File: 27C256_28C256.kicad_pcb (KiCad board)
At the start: 2 copper layers, 16.4 x 34.2 mm, 3 parts, among them J1 27C256 DIP LEGS, U1 28C256

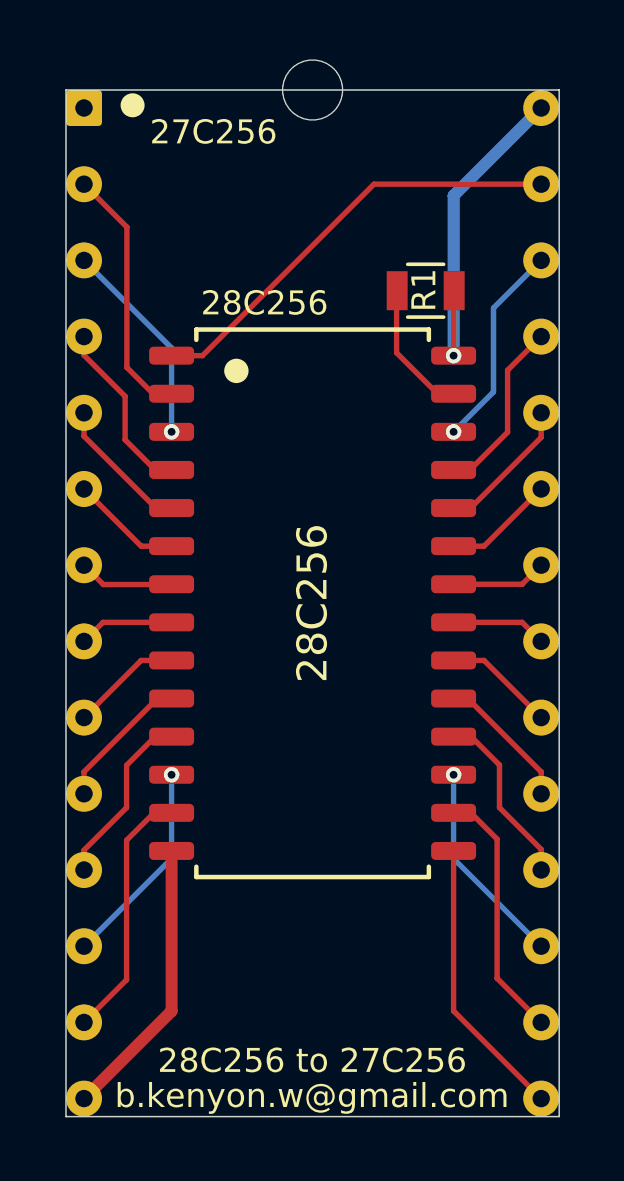
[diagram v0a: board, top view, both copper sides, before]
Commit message: 27C256_28C256: add jumpers to allow programming without needing a test clip
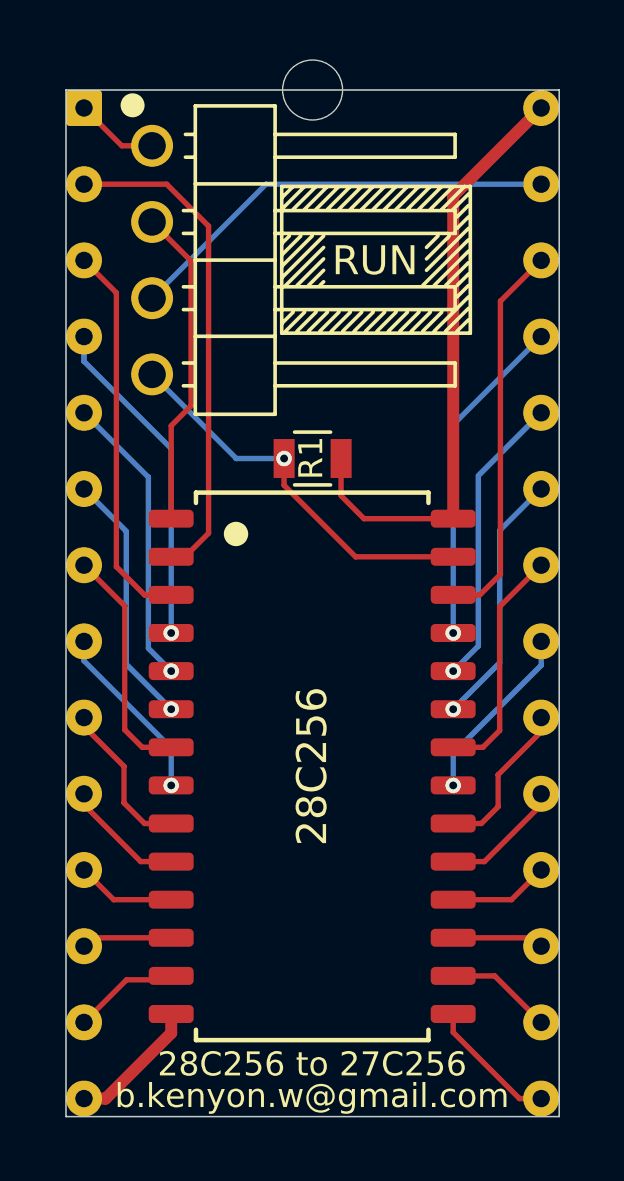
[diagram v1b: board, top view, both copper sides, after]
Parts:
- added JP1: Jumper_3_Bridged12, 000_LOCAL:Pin_Header_Angled_1x04_Pitch2.54mm, F.Cu at (144.7, 84.8)
- moved R1 6.75 mm to (150.0, 95.2)
- moved U1 5.44 mm to (150.0, 105.4)
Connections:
- J1 pad 1: (no net) -> /NC_A14
- J1 pad 27: /A14 -> /A14_WE
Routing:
- net /A14_WE: track 0.00 -> 14.5 mm
- net /VCC: track 11.6 -> 20.2 mm, vias 1 -> 0
- net /~WE: track 4.54 -> 13.1 mm, vias 0 -> 1
- net /A12: track 8.55 -> 16.5 mm
- net /A13: track 6.92 -> 12.9 mm, vias 1 -> 0
- net /A7: track 6.92 -> 12.9 mm, vias 1 -> 0
- net /A5: track 4.69 -> 9.81 mm, vias 0 -> 1
- net /A8: track 5.97 -> 11.1 mm, vias 0 -> 1
- net /A6: track 5.97 -> 11.1 mm, vias 0 -> 1
- net /A9: track 4.72 -> 9.83 mm, vias 0 -> 1
- net /GND: track 9.46 -> 4.45 mm
- net /D3: track 9.46 -> 4.46 mm
- net /D2: track 8.54 -> 3.55 mm
- net /D4: track 8.53 -> 3.57 mm
- net /A11: track 3.71 -> 8.56 mm, vias 0 -> 1
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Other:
- board text added: "27C256 pinout (RUN)"
- board text added: "28C256 pinout (PROGRAM)"
- board text added: "RUN"
- board text removed: "27C256"
- board text removed: "28C256"

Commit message: pours and text
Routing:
- net /A6: track 11.1 -> 19.0 mm
- net /A8: track 11.1 -> 13.4 mm
- net /A12: track 16.5 -> 17.8 mm
- net /A13: track 12.9 -> 13.5 mm
- net /GND: vias 0 -> 3
- added copper zone on B.Cu, net /GND
- added copper zone on F.Cu, net /GND
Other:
- board text added: "27C256 to 28C256"
- board text added: "github.com/bkw777/aDIPters"
- board text removed: "28C256 to 27C256"
- board text removed: "b.kenyon.w@gmail.com"

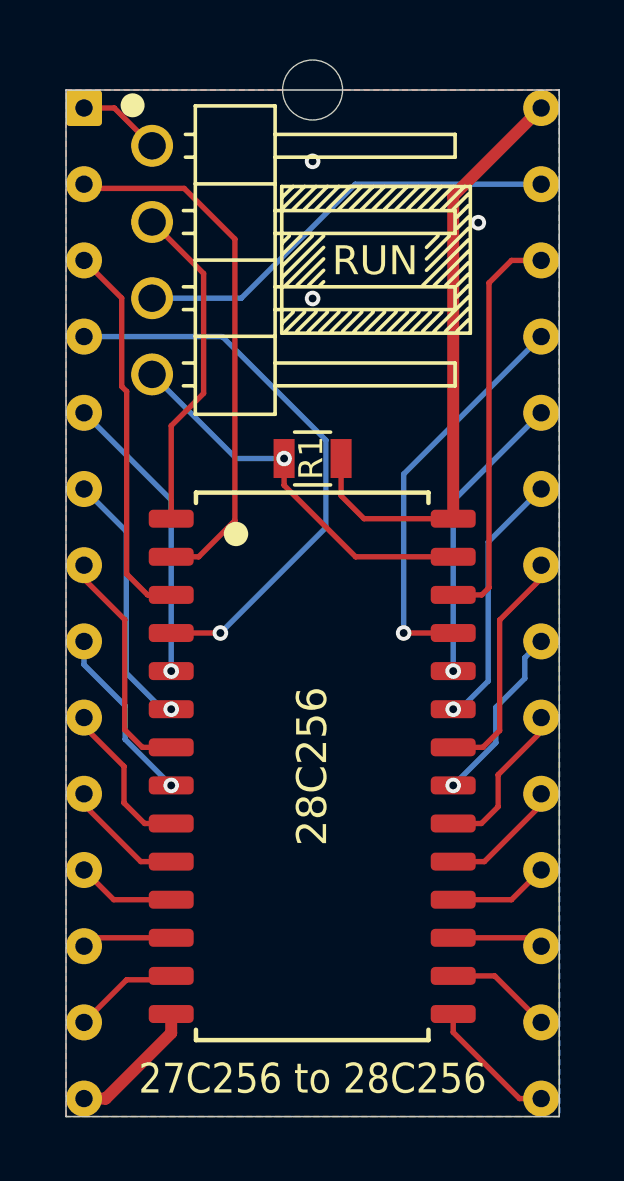
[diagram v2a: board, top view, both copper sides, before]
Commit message: improve copper pour
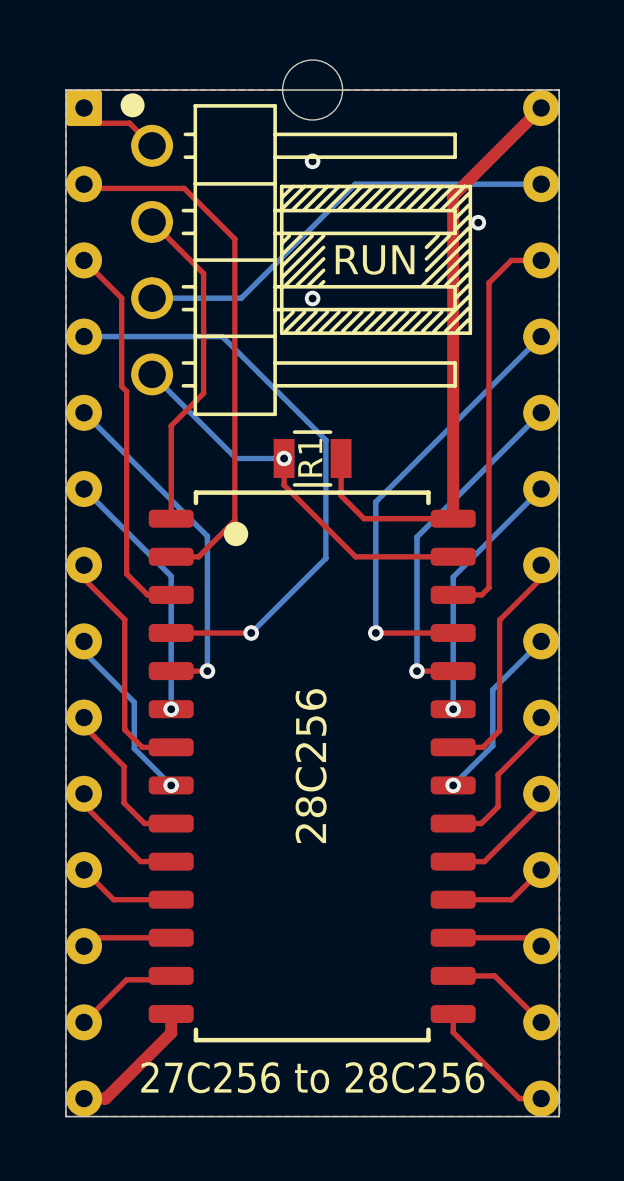
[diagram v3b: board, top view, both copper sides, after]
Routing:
- net /A9: track 9.83 -> 11.5 mm
- net /A5: track 9.81 -> 11.5 mm
- net /A8: track 13.4 -> 14.7 mm
- net /A6: track 19.0 -> 19.6 mm
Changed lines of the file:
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@@
     (thickness 1.6)
     (drawings 84)
-    (tracks 122)
+    (tracks 119)
     (zones 0)
     (modules 4)
@@
   )
   (setup
-    (last_trace_width 0.25)
+    (last_trace_width 0.18)
     (user_trace_width 0.16)
     (user_trace_width 0.18)
@@
   (segment (start 142.6596 111.1504) (end 142.38 111.43) (width 0.18) (layer F.Cu) (net 6))
   (segment (start 145.287 111.1504) (end 142.6596 111.1504) (width 0.18) (layer F.Cu) (net 6))
-  (via (at 153.035 100.9904) (size 0.52) (drill 0.26) (layers F.Cu B.Cu) (net 7))
-  (segment (start 153.035 95.695) (end 157.62 91.11) (width 0.18) (layer B.Cu) (net 7))
-  (segment (start 153.035 100.9904) (end 153.035 95.695) (width 0.18) (layer B.Cu) (net 7))
-  (segment (start 153.035 100.9904) (end 154.687 100.9904) (width 0.18) (layer F.Cu) (net 7))
+  (via (at 152.1079 100.9904) (size 0.52) (drill 0.26) (layers F.Cu B.Cu) (net 7))
+  (segment (start 152.1079 100.9904) (end 154.687 100.9904) (width 0.18) (layer F.Cu) (net 7))
+  (segment (start 152.1079 96.6221) (end 157.62 91.11) (width 0.18) (layer B.Cu) (net 7))
+  (segment (start 152.1079 100.9904) (end 152.1079 96.6221) (width 0.18) (layer B.Cu) (net 7))
   (segment (start 143.3704 109.8804) (end 145.287 109.8804) (width 0.18) (layer F.Cu) (net 8))
   (segment (start 142.38 108.89) (end 143.3704 109.8804) (width 0.18) (layer F.Cu) (net 8))
-  (via (at 154.687 102.2604) (size 0.52) (drill 0.26) (layers F.Cu B.Cu) (net 9))
-  (segment (start 154.687 96.583) (end 157.62 93.65) (width 0.18) (layer B.Cu) (net 9))
-  (segment (start 154.687 102.2604) (end 154.687 96.583) (width 0.18) (layer B.Cu) (net 9))
+  (via (at 153.4795 102.2604) (size 0.52) (drill 0.26) (layers F.Cu B.Cu) (net 9))
+  (segment (start 153.4795 102.2604) (end 154.687 102.2604) (width 0.18) (layer F.Cu) (net 9))
+  (segment (start 153.4795 97.7905) (end 157.62 93.65) (width 0.18) (layer B.Cu) (net 9))
+  (segment (start 153.4795 102.2604) (end 153.4795 97.7905) (width 0.18) (layer B.Cu) (net 9))
   (segment (start 142.38 106.7184) (end 142.38 106.35) (width 0.18) (layer F.Cu) (net 10))
   (segment (start 145.287 108.6104) (end 144.272 108.6104) (width 0.18) (layer F.Cu) (net 10))
   (segment (start 144.272 108.6104) (end 142.38 106.7184) (width 0.18) (layer F.Cu) (net 10))
   (via (at 154.687 103.5304) (size 0.52) (drill 0.26) (layers F.Cu B.Cu) (net 11))
-  (segment (start 155.8544 102.5906) (end 155.8544 97.9556) (width 0.18) (layer B.Cu) (net 11))
-  (segment (start 154.687 103.5304) (end 154.9146 103.5304) (width 0.18) (layer B.Cu) (net 11))
-  (segment (start 155.8544 97.9556) (end 157.62 96.19) (width 0.18) (layer B.Cu) (net 11))
-  (segment (start 154.9146 103.5304) (end 155.8544 102.5906) (width 0.18) (layer B.Cu) (net 11))
+  (segment (start 154.687 99.123) (end 157.62 96.19) (width 0.18) (layer B.Cu) (net 11))
+  (segment (start 154.687 103.5304) (end 154.687 99.123) (width 0.18) (layer B.Cu) (net 11))
   (segment (start 143.7132 105.4354) (end 142.38 104.1022) (width 0.18) (layer F.Cu) (net 12))
   (segment (start 142.38 104.1022) (end 142.38 103.81) (width 0.18) (layer F.Cu) (net 12))
@@
   (segment (start 155.6766 104.8004) (end 156.2354 104.2416) (width 0.18) (layer F.Cu) (net 13))
   (via (at 145.287 106.0704) (size 0.52) (drill 0.26) (layers F.Cu B.Cu) (net 14))
-  (segment (start 142.38 102.0448) (end 142.38 101.27) (width 0.18) (layer B.Cu) (net 14))
-  (segment (start 143.7513 103.4161) (end 142.38 102.0448) (width 0.18) (layer B.Cu) (net 14))
-  (segment (start 145.287 106.0704) (end 143.7513 104.5347) (width 0.18) (layer B.Cu) (net 14))
-  (segment (start 143.7513 104.5347) (end 143.7513 103.4161) (width 0.18) (layer B.Cu) (net 14))
+  (segment (start 142.38 101.6257) (end 142.38 101.27) (width 0.18) (layer B.Cu) (net 14))
+  (segment (start 144.0561 103.3018) (end 142.38 101.6257) (width 0.18) (layer B.Cu) (net 14))
+  (segment (start 145.287 106.0704) (end 144.0561 104.8395) (width 0.18) (layer B.Cu) (net 14))
+  (segment (start 144.0561 104.8395) (end 144.0561 103.3018) (width 0.18) (layer B.Cu) (net 14))
   (via (at 154.687 106.0704) (size 0.52) (drill 0.26) (layers F.Cu B.Cu) (net 15))
-  (segment (start 157.0736 102.5017) (end 157.0736 101.8164) (width 0.18) (layer B.Cu) (net 15))
-  (segment (start 156.1084 103.4669) (end 157.0736 102.5017) (width 0.18) (layer B.Cu) (net 15))
-  (segment (start 154.687 106.0704) (end 156.1084 104.649) (width 0.18) (layer B.Cu) (net 15))
-  (segment (start 157.0736 101.8164) (end 157.62 101.27) (width 0.18) (layer B.Cu) (net 15))
-  (segment (start 156.1084 104.649) (end 156.1084 103.4669) (width 0.18) (layer B.Cu) (net 15))
+  (segment (start 156.0068 102.8832) (end 157.62 101.27) (width 0.18) (layer B.Cu) (net 15))
+  (segment (start 154.687 106.0704) (end 156.0068 104.7506) (width 0.18) (layer B.Cu) (net 15))
+  (segment (start 156.0068 104.7506) (end 156.0068 102.8832) (width 0.18) (layer B.Cu) (net 15))
   (segment (start 142.38 99.1873) (end 142.38 98.73) (width 0.18) (layer F.Cu) (net 16))
   (segment (start 143.7386 100.5459) (end 142.38 99.1873) (width 0.18) (layer F.Cu) (net 16))
@@
   (segment (start 155.6258 107.3404) (end 156.1846 106.7816) (width 0.18) (layer F.Cu) (net 17))
   (via (at 145.287 103.5304) (size 0.52) (drill 0.26) (layers F.Cu B.Cu) (net 18))
-  (segment (start 143.7894 97.5994) (end 142.38 96.19) (width 0.18) (layer B.Cu) (net 18))
-  (segment (start 145.287 103.5304) (end 144.9959 103.5304) (width 0.18) (layer B.Cu) (net 18))
-  (segment (start 143.7894 102.3239) (end 143.7894 97.5994) (width 0.18) (layer B.Cu) (net 18))
-  (segment (start 144.9959 103.5304) (end 143.7894 102.3239) (width 0.18) (layer B.Cu) (net 18))
+  (segment (start 145.287 99.097) (end 142.38 96.19) (width 0.18) (layer B.Cu) (net 18))
+  (segment (start 145.287 103.5304) (end 145.287 99.097) (width 0.18) (layer B.Cu) (net 18))
   (segment (start 157.62 106.7178) (end 157.62 106.35) (width 0.18) (layer F.Cu) (net 19))
   (segment (start 154.687 108.6104) (end 155.7274 108.6104) (width 0.18) (layer F.Cu) (net 19))
   (segment (start 155.7274 108.6104) (end 157.62 106.7178) (width 0.18) (layer F.Cu) (net 19))
-  (via (at 145.287 102.2604) (size 0.52) (drill 0.26) (layers F.Cu B.Cu) (net 20))
-  (segment (start 145.287 96.557) (end 142.38 93.65) (width 0.18) (layer B.Cu) (net 20))
-  (segment (start 145.287 102.2604) (end 145.287 96.557) (width 0.18) (layer B.Cu) (net 20))
+  (via (at 146.4945 102.2604) (size 0.52) (drill 0.26) (layers F.Cu B.Cu) (net 20))
+  (segment (start 146.4945 102.2604) (end 145.287 102.2604) (width 0.18) (layer F.Cu) (net 20))
+  (segment (start 146.4945 97.7645) (end 142.38 93.65) (width 0.18) (layer B.Cu) (net 20))
+  (segment (start 146.4945 102.2604) (end 146.4945 97.7645) (width 0.18) (layer B.Cu) (net 20))
   (segment (start 156.6296 109.8804) (end 157.62 108.89) (width 0.18) (layer F.Cu) (net 21))
   (segment (start 154.687 109.8804) (end 156.6296 109.8804) (width 0.18) (layer F.Cu) (net 21))
-  (via (at 146.9263 100.9904) (size 0.52) (drill 0.26) (layers F.Cu B.Cu) (net 22))
-  (segment (start 145.287 100.9904) (end 146.9263 100.9904) (width 0.18) (layer F.Cu) (net 22))
+  (segment (start 145.287 100.9904) (end 147.955 100.9904) (width 0.18) (layer F.Cu) (net 22))
+  (via (at 147.955 100.9904) (size 0.52) (drill 0.26) (layers F.Cu B.Cu) (net 22))
   (segment (start 146.99 91.11) (end 142.38 91.11) (width 0.18) (layer B.Cu) (net 22))
   (segment (start 150.4442 94.5642) (end 146.99 91.11) (width 0.18) (layer B.Cu) (net 22))
-  (segment (start 146.9263 100.9904) (end 150.4442 97.4725) (width 0.18) (layer B.Cu) (net 22))
-  (segment (start 150.4442 97.4725) (end 150.4442 94.5642) (width 0.18) (layer B.Cu) (net 22))
+  (segment (start 147.955 100.9904) (end 150.4442 98.5012) (width 0.18) (layer B.Cu) (net 22))
+  (segment (start 150.4442 98.5012) (end 150.4442 94.5642) (width 0.18) (layer B.Cu) (net 22))
   (segment (start 157.3404 111.1504) (end 157.62 111.43) (width 0.18) (layer F.Cu) (net 23))
   (segment (start 154.687 111.1504) (end 157.3404 111.1504) (width 0.18) (layer F.Cu) (net 23))
@@
   (segment (start 157.62 86.03) (end 151.4219 86.03) (width 0.18) (layer B.Cu) (net 29))
   (segment (start 151.4219 86.03) (end 147.6219 89.83) (width 0.18) (layer B.Cu) (net 29))
-  (segment (start 143.39 83.49) (end 142.38 83.49) (width 0.18) (layer F.Cu) (net 30))
-  (segment (start 144.65 84.75) (end 143.39 83.49) (width 0.18) (layer F.Cu) (net 30))
+  (segment (start 142.8878 83.9978) (end 142.38 83.49) (width 0.18) (layer F.Cu) (net 30))
+  (segment (start 144.65 84.75) (end 143.8978 83.9978) (width 0.18) (layer F.Cu) (net 30))
+  (segment (start 143.8978 83.9978) (end 142.8878 83.9978) (width 0.18) (layer F.Cu) (net 30))
   (zone (net 2) (net_name /GND) (layer F.Cu) (hatch edge 0.508)
     (connect_pads (clearance 0.1524))

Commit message: minor touches
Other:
- board text added: "28C256 to 27C256"
- board text removed: "27C256 to 28C256"
